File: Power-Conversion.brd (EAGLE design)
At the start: 160 x 81.3 mm, 55 parts, among them J1 AVR_SPI_PRG_6PTH, U1 ATMEGA328P_TQFP, U2 LM1085IS-3.3

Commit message: add 1"
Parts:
- moved F1 25.4 mm to (76.2, 16.5)
- moved F2 25.4 mm to (76.2, 67.3)
- moved F3 25.4 mm to (76.2, 29.2)
- moved F5 25.4 mm to (76.2, 41.9)
- moved F7 25.4 mm to (76.2, 54.6)
- moved R1 25.4 mm to (121.9, 39.4)
- moved U$1 25.4 mm to (180.3, 38.1)
- moved U$4 25.4 mm to (118.1, 39.4)
- moved U$5 25.4 mm to (121.9, 43.2)
- moved U$7 25.4 mm to (113.0, 44.5)
- moved R4 25.4 mm to (29.6, 66.0)
- moved V+_ESC1 25.4 mm to (53.3, 12.7)
- moved V+_ESC3 25.4 mm to (53.3, 25.4)
- moved V+_ESC5 25.4 mm to (53.3, 38.1)
- moved V+_ESC7 25.4 mm to (53.3, 50.8)
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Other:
- board size 160 x 81.3 mm -> 185.4 x 81.3 mm

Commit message: stuffs
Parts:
- added F4: (no value), MotherboardParts:KEYSTONE_FUSE_3587
- added I2C_ESC11, I2C_ESC12: (no value), SparkFun-Connectors:1X01
- added V+_CONN, V+_ESC11, V+_ESC12, V-_CONN, V-_ESC11, V-_ESC12: (no value), SparkFun-Connectors:BANANA_CONN
- moved V-_ESC1 5.08 mm to (49.5, 12.7)
- moved V-_ESC3 5.08 mm to (49.5, 25.4)
- moved V-_ESC5 5.08 mm to (49.5, 38.1)
- moved V-_ESC7 5.08 mm to (49.5, 50.8)
- moved V-_ESC9 5.08 mm to (49.5, 63.5)
- moved V-_ESC10 4.02 mm to (53.3, 69.8)
- moved V-_ESC4 4.02 mm to (53.3, 31.8)
- moved V-_ESC8 4.02 mm to (53.3, 57.1)
- moved V-_ESC2 4.02 mm to (53.3, 19.1)
- moved V-_ESC6 4.02 mm to (53.3, 44.5)
- moved V+_ESC1 3.81 mm to (57.1, 12.7)
- moved V+_ESC3 3.81 mm to (57.1, 25.4)
- moved V+_ESC5 3.81 mm to (57.1, 38.1)
- moved V+_ESC7 3.81 mm to (57.1, 50.8)
- moved V+_ESC9 3.81 mm to (57.1, 63.5)
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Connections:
- new net N$2: I2C_ESC11.1, U$8.P$17
- new net N$4: I2C_ESC12.1, U$8.P$18
- new net N$6: F4.P$3, F4.P$4, V+_ESC11.P$1, V+_ESC12.P$1
- net GND: now also V-_ESC11.P$1, V-_ESC12.P$1
- net V+: now also V+_CONN.P$1
- net V-: now also V-_CONN.P$1
- net VCC: now also F4.P$1, F4.P$2
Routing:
- net VCC: track 59.6 -> 6.45 mm
- net N$15: track 48.2 -> 39.3 mm
- net N$16: track 40.3 -> 32.6 mm
- net N$21: track 8.52 -> 0.90 mm
- net N$17: track 35.0 -> 28.4 mm
- net N$18: track 27.1 -> 21.9 mm
- net N$24: track 9.03 -> 4.20 mm
- net N$19: track 21.8 -> 18.0 mm
- net N$22: track 2.97 -> 0.00 mm
- net N$23: track 2.76 -> 0.00 mm
- net N$20: track 13.9 -> 11.4 mm

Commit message: Fuse
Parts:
- removed I2C_ESC1, I2C_ESC10, I2C_ESC11, I2C_ESC12, I2C_ESC2, I2C_ESC3, I2C_ESC4, I2C_ESC5, I2C_ESC6, I2C_ESC7, I2C_ESC8, I2C_ESC9: (no value), SparkFun-Connectors:1X01
- added PWM_ESC1, PWM_ESC10, PWM_ESC11, PWM_ESC12, PWM_ESC2, PWM_ESC3, PWM_ESC4, PWM_ESC5, PWM_ESC6, PWM_ESC7, PWM_ESC8, PWM_ESC9: (no value), SparkFun-Connectors:1X01
- moved V-_CONN 323.7 mm to (133.3, 45.7)
- moved V+_CONN 266.0 mm to (128.3, 40.6)
- moved F4 251.4 mm to (76.2, 72.4), turned to 180 degrees
- moved V-_ESC12 211.6 mm to (53.3, 74.9)
- moved V-_ESC11 204.3 mm to (49.5, 68.6)
- moved V+_ESC12 156.4 mm to (61.0, 74.9)
- moved V+_ESC11 151.4 mm to (57.1, 68.6)
- moved F2 7.62 mm to (76.2, 59.7)
- moved V+_ESC6 7.62 mm to (61.0, 36.8)
- moved V-_ESC6 7.62 mm to (53.3, 36.8)
- moved F1 7.62 mm to (76.2, 8.89)
- moved F3 7.62 mm to (76.2, 21.6)
- moved V+_ESC2 7.62 mm to (61.0, 11.4)
- moved V+_ESC4 7.62 mm to (61.0, 24.1)
- moved V+_ESC5 7.62 mm to (57.1, 30.5)
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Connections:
- net N$15: now also PWM_ESC1.1; no longer I2C_ESC1.1
- net N$16: now also PWM_ESC2.1; no longer I2C_ESC2.1
- net N$17: now also PWM_ESC3.1; no longer I2C_ESC3.1
- net N$18: now also PWM_ESC4.1; no longer I2C_ESC4.1
- net N$19: now also PWM_ESC5.1; no longer I2C_ESC5.1
- net N$2: now also PWM_ESC11.1; no longer I2C_ESC11.1
- net N$20: now also PWM_ESC6.1; no longer I2C_ESC6.1
- net N$21: now also PWM_ESC7.1; no longer I2C_ESC7.1
- net N$22: now also PWM_ESC8.1; no longer I2C_ESC8.1
- net N$23: now also PWM_ESC9.1; no longer I2C_ESC9.1
- net N$24: now also PWM_ESC10.1; no longer I2C_ESC10.1
- net N$4: now also PWM_ESC12.1; no longer I2C_ESC12.1
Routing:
- net SDA: track 202.7 -> 131.0 mm
- net SCL: track 211.8 -> 145.8 mm
- added copper zone on layer 1, net N$6

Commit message: Here goes nothin
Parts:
- moved V-_CONN 43.7 mm to (94.0, 64.8), turned to 180 degrees
- moved V+_CONN 41.3 mm to (99.1, 69.8), turned to 180 degrees
- moved R1 35.8 mm to (105.4, 71.1), turned to 90 degrees
- moved U$3 33.4 mm to (106.7, 35.6)
- moved U$4 33.0 mm to (109.2, 71.1), turned to 270 degrees
- moved R2 32.4 mm to (116.8, 71.1), turned to 180 degrees
- moved U$6 31.8 mm to (113.0, 71.1), turned to 270 degrees
- moved U$2 29.7 mm to (111.8, 43.2)
- moved U$1 29.2 mm to (151.1, 39.4)
- moved U$5 29.2 mm to (105.4, 67.3), turned to 180 degrees
- moved F1 24.1 mm to (52.1, 8.89)
- moved F2 24.1 mm to (52.1, 59.7)
- moved F3 24.1 mm to (52.1, 21.6)
- moved F4 24.1 mm to (52.1, 72.4)
- moved F5 24.1 mm to (52.1, 34.3)
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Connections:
- net SCL: now also U$1.P$54, U$2.P$54, U$3.P$54; no longer U$1.P$53, U$2.P$53, U$3.P$53
- net SDA: now also U$1.P$53, U$2.P$53, U$3.P$53; no longer U$1.P$54, U$2.P$54, U$3.P$54
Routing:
- net ONOFF: track 184.4 -> 16.4 mm
- net SCL: track 145.8 -> 5.15 mm
- net SDA: track 131.0 -> 3.61 mm
- net V+: track 31.4 -> 1.86 mm
- net GND: track 27.6 -> 22.5 mm
- net V-: track 28.8 -> 25.5 mm
- removed copper zone on layer 1, net V+
- removed copper zone on layer 16, net V-

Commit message: redesign
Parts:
- moved C1 125.7 mm to (131.7, 40.5)
- moved C2 125.7 mm to (131.7, 38.9)
- moved C3 125.7 mm to (129.4, 66.0)
- moved R5 125.7 mm to (131.3, 55.5)
- moved U$8 125.7 mm to (134.0, 60.7)
- moved J1 125.7 mm to (130.0, 9.14)
- moved R3 125.7 mm to (137.3, 39.8)
- moved R4 125.7 mm to (131.2, 66.0)
- moved R6 125.7 mm to (132.7, 55.5)
- moved U1 125.7 mm to (133.0, 46.5)
- moved U2 125.7 mm to (133.3, 29.7)
- moved V-_CONN 68.4 mm to (160.0, 47.0)
- moved V+_CONN 68.2 mm to (160.0, 39.4)
- moved U$2 62.3 mm to (49.5, 39.4), turned to 180 degrees
- moved F1 15.2 mm to (36.8, 8.89)
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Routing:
- net GND: track 22.5 -> 17.4 mm
- removed copper zone on layer 1, net VCC

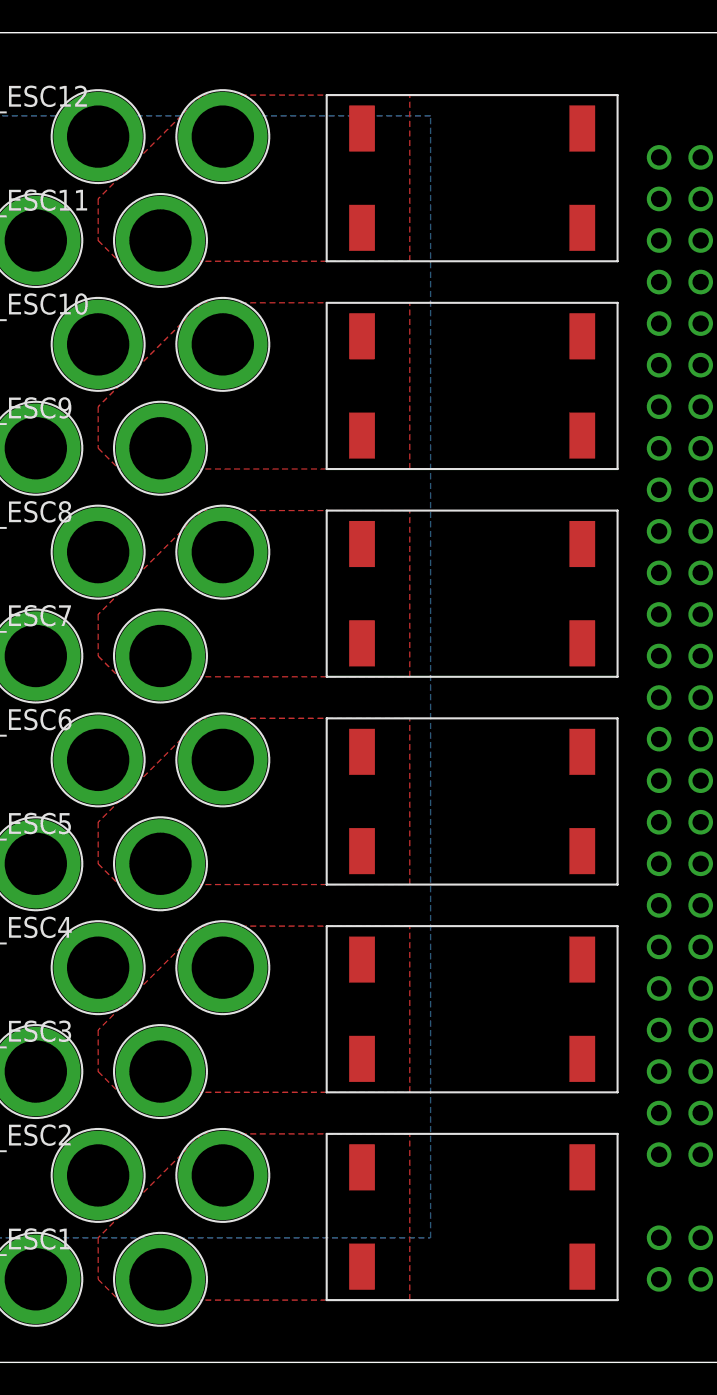
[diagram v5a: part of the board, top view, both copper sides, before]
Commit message: Replaced normal fuses with individual PTC fuses
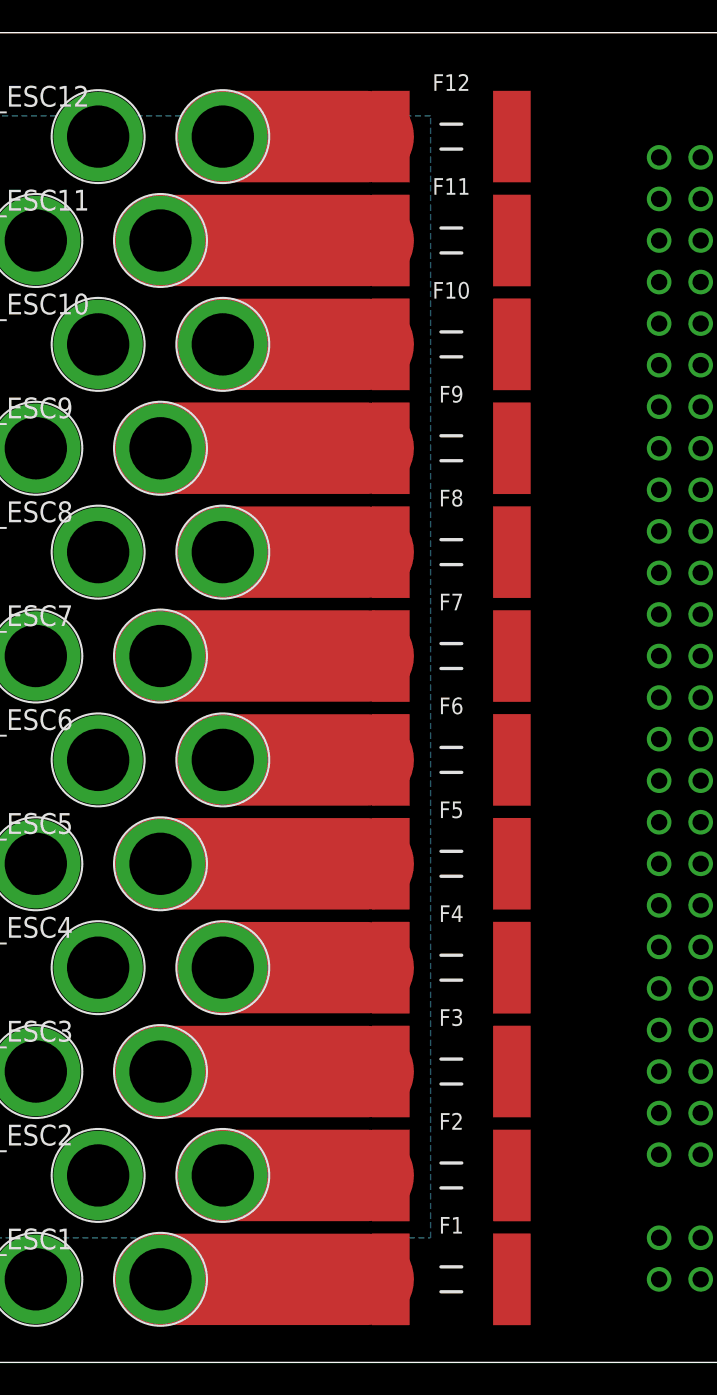
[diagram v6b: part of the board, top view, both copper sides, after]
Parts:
- added F10, F11, F12, F6, F8, F9: 10A, PowerComponents:PTC-2920
- F1, F2, F3, F4, F5, F7: value (none) -> 10A; device MotherboardParts:KEYSTONE_FUSE_3587 -> PowerComponents:PTC-2920
- moved F4 48.3 mm to (35.6, 24.1), turned to 0 degrees
- moved F2 48.3 mm to (35.6, 11.4), turned to 0 degrees
- moved F7 4.02 mm to (35.6, 43.2), turned to 0 degrees
- moved F1 4.02 mm to (35.6, 5.08), turned to 0 degrees
- moved F3 4.02 mm to (35.6, 17.8), turned to 0 degrees
- moved F5 4.02 mm to (35.6, 30.5), turned to 0 degrees
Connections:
- new net N$28: F9.1, V+_ESC9.P$1
- new net N$30: F10.1, V+_ESC10.P$1
- new net N$32: F4.1, V+_ESC4.P$1
- new net N$33: F11.1, V+_ESC11.P$1
- new net N$34: F12.1, V+_ESC12.P$1
- new net N$8: F7.1, V+_ESC7.P$1
- net N$1: now also F1.1; no longer F1.P$3, F1.P$4, V+_ESC2.P$1
- net N$11: now also F8.1, V+_ESC8.P$1; no longer F2.P$3, F2.P$4, V+_ESC10.P$1, V+_ESC9.P$1
- net N$3: now also F2.1, V+_ESC2.P$1; no longer F3.P$3, F3.P$4, V+_ESC3.P$1, V+_ESC4.P$1
- net N$5: now also F3.1, V+_ESC3.P$1; no longer F5.P$3, F5.P$4, V+_ESC5.P$1, V+_ESC6.P$1
- net N$6: now also F5.1, V+_ESC5.P$1; no longer F4.P$3, F4.P$4, V+_ESC11.P$1, V+_ESC12.P$1
- net N$7: now also F6.1, V+_ESC6.P$1; no longer F7.P$3, F7.P$4, V+_ESC7.P$1, V+_ESC8.P$1
- net VCC: now also F1.2, F10.2, F11.2, F12.2, F2.2, F3.2, F4.2, F5.2, F6.2, F7.2, F8.2, F9.2; no longer F1.P$1, F1.P$2, F2.P$1, F2.P$2, F3.P$1, F3.P$2, F4.P$1, F4.P$2, F5.P$1, F5.P$2, F7.P$1, F7.P$2
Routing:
- net N$8: track 0.00 -> 14.1 mm
- net N$6: track 0.00 -> 14.1 mm
- net N$5: track 0.00 -> 14.1 mm
- net N$33: track 0.00 -> 14.1 mm
- net N$28: track 0.00 -> 14.1 mm
- net N$1: track 0.00 -> 14.1 mm
- net N$7: track 0.00 -> 10.3 mm
- net N$34: track 0.00 -> 10.3 mm
- net N$32: track 0.00 -> 10.3 mm
- net N$30: track 0.00 -> 10.3 mm
- net N$3: track 0.00 -> 10.3 mm
- net N$11: track 0.00 -> 10.3 mm
- removed copper zone on layer 1, net N$1
- removed copper zone on layer 1, net N$11
- removed copper zone on layer 1, net N$3
- removed copper zone on layer 1, net N$5
- removed copper zone on layer 1, net N$6
- removed copper zone on layer 1, net N$7

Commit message: After 8 hours of continuous work, I am 90% done with the power distribution board
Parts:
- added C4, C5: 1uF, SparkFun-Capacitors:0603-CAP
- added ESC_GND1, ESC_GND10, ESC_GND11, ESC_GND12, ESC_GND2, ESC_GND3, ESC_GND4, ESC_GND5, ESC_GND6, ESC_GND7, ESC_GND8, ESC_GND9: (no value), SparkFun-Connectors:1X01
- added U$9: FT230XS, USB-UART:SSOP-16
- added U3: LM1085IS-3.3, PowerComponents:TO254P1435X457-3N
- moved J1 68.9 mm to (142.2, 77.0), turned to 270 degrees
- moved R2 55.4 mm to (63.8, 36.1), turned to 0 degrees
- moved U$7 51.5 mm to (66.3, 44.5), turned to 90 degrees
- moved U$6 48.1 mm to (70.1, 36.1), turned to 90 degrees
- moved V-_CONN 47.3 mm to (112.8, 46.0)
- moved U$4 41.6 mm to (75.7, 35.8), turned to 90 degrees
- moved V+_CONN 39.7 mm to (120.4, 40.9)
- moved R3 36.7 mm to (129.3, 75.6), turned to 180 degrees
- moved R1 34.3 mm to (82.0, 35.8), turned to 270 degrees
- moved U$5 32.5 mm to (81.8, 44.5), turned to 180 degrees
- moved C2 27.0 mm to (144.0, 62.9), turned to 270 degrees
- moved U2 26.1 mm to (110.4, 17.3), turned to 90 degrees
- moved R6 23.4 mm to (129.3, 78.6), turned to 0 degrees
- moved C1 22.2 mm to (128.3, 62.5), turned to 270 degrees
- moved R5 21.7 mm to (129.3, 77.1), turned to 0 degrees
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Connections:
- new net +5_SERVO: C4.1, U2.2, U2.4
- net +5V: now also C5.1, U3.2, U3.4; no longer U2.2, U2.4
- net GND: now also C4.2, C5.2, ESC_GND1.1, ESC_GND10.1, ESC_GND11.1, ESC_GND12.1, ESC_GND2.1, ESC_GND3.1, ESC_GND4.1, ESC_GND5.1, ESC_GND6.1, ESC_GND7.1, ESC_GND8.1, ESC_GND9.1, U$9.P$13, U$9.P$5, U3.1
- net VCC: now also U3.3
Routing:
- net SDA: track 3.61 -> 174.0 mm
- net SCL: track 5.15 -> 174.4 mm
- net N$15: track 39.3 -> 203.4 mm
- net N$16: track 32.6 -> 186.1 mm
- net ONOFF: track 16.4 -> 167.7 mm
- net N$21: track 0.90 -> 151.9 mm, vias 0 -> 1
- net N$18: track 21.9 -> 172.1 mm
- net N$19: track 18.0 -> 168.2 mm
- net N$17: track 28.4 -> 178.4 mm
- net N$20: track 11.4 -> 160.8 mm
- net N$22: track 0.00 -> 144.8 mm, vias 0 -> 1
- net N$23: track 0.00 -> 142.7 mm, vias 0 -> 1
- net N$2: track 0.00 -> 135.3 mm, vias 0 -> 1
- net N$4: track 0.00 -> 134.5 mm, vias 0 -> 1
- net N$24: track 4.20 -> 137.5 mm, vias 0 -> 1
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- added copper zone on layer 15, net GND
- added copper zone on layer 2, net GND
- added copper zone on layer 16, net V+
- added copper zone on layer 16, net V-
- added copper zone on layer 1, net VCC
- added copper zone on layer 16, net VCC
- removed copper zone on layer 1, net +5V
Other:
- board size 185.4 x 81.3 mm -> 185.4 x 81 mm

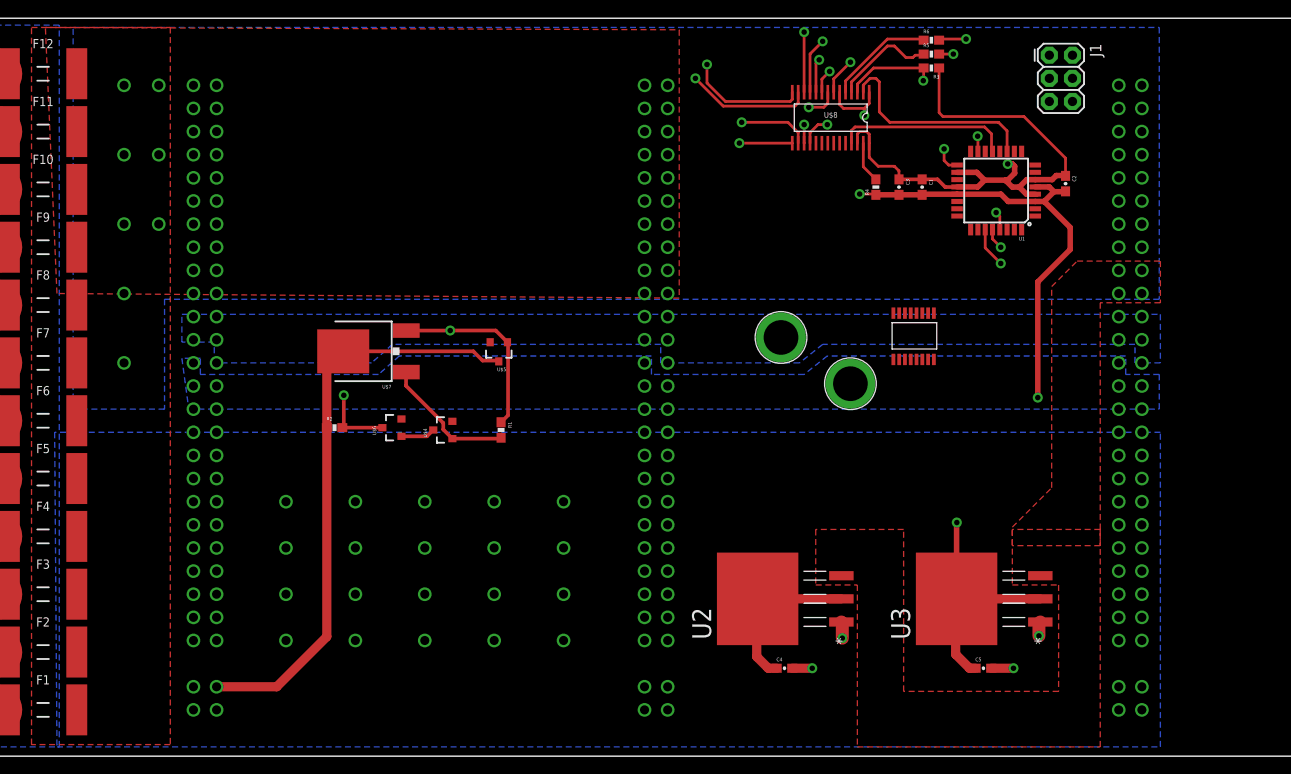
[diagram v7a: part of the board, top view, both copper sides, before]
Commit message: Finished most of the wiring.  Also changed pwm chips and FTDI chips
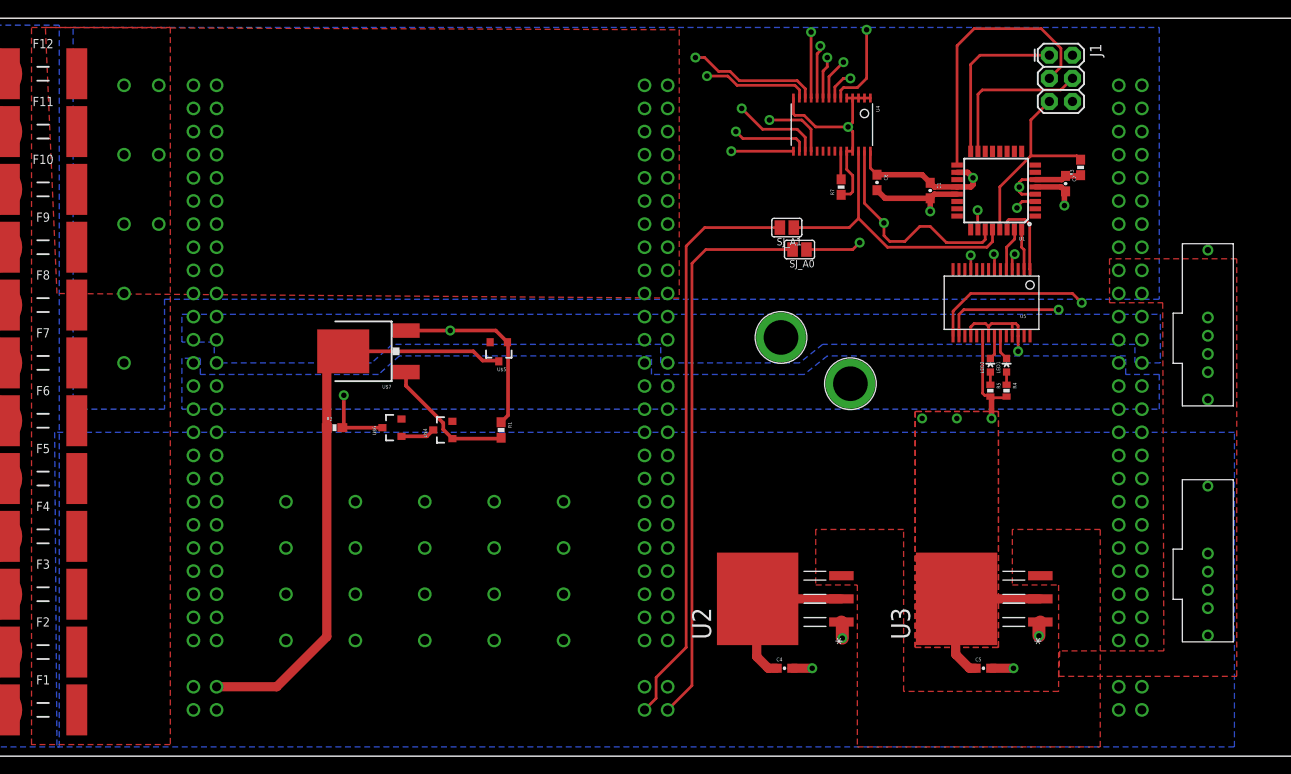
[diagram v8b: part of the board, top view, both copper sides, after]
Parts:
- removed C3: 0.1uF, SparkFun-Capacitors:0603-CAP
- removed R6: 470, SparkFun-Resistors:0603-RES
- removed U$8: TLC59401PWPR, MotherboardParts:TLC59401PWPR
- removed U$9: FT230XS, USB-UART:SSOP-16
- added C6: 10uF, SparkFun-Capacitors:0603-CAP
- added CAMDATA, CAMDATA1: T2I, BACKPLANE:T2I
- added LED1: Red, SparkFun:LED-0603
- added LED2: Green, SparkFun:LED-0603
- added R7: 10k, SparkFun-Resistors:0603-RES
- added SJ_A0, SJ_A1: (no value), microbuilder:SOLDERJUMPER_REFLOW_NOPASTE
- added U4: PCA9685, microbuilder:TSSOP28
- added U5: FT232RLSSOP, SparkFun:SSOP28DB
- R4: device SparkFun-Resistors:0603-RES -> SparkFun:0402-RES
- R5: value 470 -> 1K; device SparkFun-Resistors:0603-RES -> SparkFun:0402-RES
- moved R5 37.5 mm to (135.8, 40.1), turned to 270 degrees
- moved R4 26.6 mm to (137.5, 40.1), turned to 270 degrees
- moved R3 19.7 mm to (145.7, 64.6), turned to 90 degrees
- moved C1 0.97 mm to (129.2, 62.1)
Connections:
- removed net N$25: R4.2, U$8.P$27
- new net CTS: U1.26, U5.11
- new net DTR: U1.32, U5.2
- new net N$35: R7.2, U4.23
- new net RXI: U1.31, U5.5
- new net RXLED: LED2.C, U5.22
- new net SCL1: SJ_A1.2, U$1.P$54, U$2.P$54, U$3.P$54
- new net SDA1: SJ_A0.2, U$1.P$53, U$2.P$53, U$3.P$53
- new net TXLED: LED1.C, U5.23
- new net TXO: U1.30, U5.1
- new net USB_D+: CAMDATA1.1, U5.15
- new net USB_D-: CAMDATA1.2, U5.16
- net +5V: now also C6.1, R4.2, R5.2, U4.28, U5.20, U5.4; no longer C3.1, U$8.P$26, U$8.P$28
- net GND: now also C6.2, CAMDATA.2, CAMDATA.3, CAMDATA.4, R7.1, U4.1, U4.14, U4.2, U4.24, U4.25, U4.3, U4.4, U4.5, U5.18, U5.21, U5.25, U5.26, U5.7; no longer C3.2, R4.1, U$8.P$1, U$8.P$6, U$9.P$13, U$9.P$5
- net GSCLK: no longer U$8.P$25
- net N$12: now also LED1.A, R4.1; no longer R5.1, U$8.P$4
- net N$13: no longer U$8.P$3
- net N$14: now also LED2.A, R5.1; no longer R6.1, U$8.P$5
- net N$15: now also U4.6; no longer U$8.P$7
- net N$16: now also U4.7; no longer U$8.P$8
- net N$17: now also U4.8; no longer U$8.P$9
- net N$18: now also U4.9; no longer U$8.P$10
- net N$19: now also U4.10; no longer U$8.P$11
- net N$2: now also U4.17; no longer U$8.P$17
- net N$20: now also U4.11; no longer U$8.P$12
- net N$21: now also U4.12; no longer U$8.P$13
- net N$22: now also U4.13; no longer U$8.P$14
- net N$23: now also U4.15; no longer U$8.P$15
- net N$24: now also U4.16; no longer U$8.P$16
- net N$26: no longer R6.2
- net N$27: no longer U$8.P$2
- net N$31: no longer R5.2
- net N$4: now also U4.18; no longer U$8.P$18
- net SCL: now also SJ_A1.1, U4.26; no longer U$1.P$54, U$2.P$54, U$3.P$54
- net SDA: now also SJ_A0.1, U4.27; no longer U$1.P$53, U$2.P$53, U$3.P$53
- net VCC: now also CAMDATA.1, CAMDATA1.3, CAMDATA1.4
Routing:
- net SCL1: track 0.00 -> 167.7 mm
- net SDA1: track 0.00 -> 165.5 mm
- net SCL: track 174.4 -> 32.5 mm, vias 1 -> 0
- net SDA: track 174.0 -> 33.9 mm, vias 1 -> 2
- net +5V: track 130.4 -> 58.7 mm, vias 2 -> 6
- net USB_D+: track 0.00 -> 32.6 mm, vias 0 -> 1
- net USB_D-: track 0.00 -> 31.1 mm, vias 0 -> 1
- net N$27: track 23.4 -> 0.00 mm
- net GND: track 84.4 -> 64.0 mm, vias 27 -> 30
- net GSCLK: track 19.2 -> 0.00 mm
- net N$29: track 0.00 -> 18.6 mm
- net N$31: track 15.3 -> 30.0 mm, vias 2 -> 0
- net N$13: track 33.3 -> 22.0 mm, vias 2 -> 0
- net N$14: track 11.8 -> 1.39 mm
- net N$12: track 11.4 -> 1.39 mm
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- added copper zone on layer 1, net +5V
- added copper zone on layer 15, net +5V
